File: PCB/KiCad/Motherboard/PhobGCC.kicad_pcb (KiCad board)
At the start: 2 copper layers, 125.5 x 72.9 mm, 60 parts, among them J1 Conn_01x06_Female, J2 Conn_01x04_Female, J3 Conn_01x01_Male, J5 Rumble, Q1 Q_NMOS_GSD, Q2 Q_PMOS_GDS, Q3 Q_NMOS_GSD, SW1 A, SW10 Dup, SW11 Dright, SW12 Ddown, SW2 B, SW3 X, SW4 Y, SW5 Start, SW6 L, SW7 R, SW8 Z, SW9 Dleft, U1 Teensy4.0, U2 2x DRV5053CAQLPGM Hall Effect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

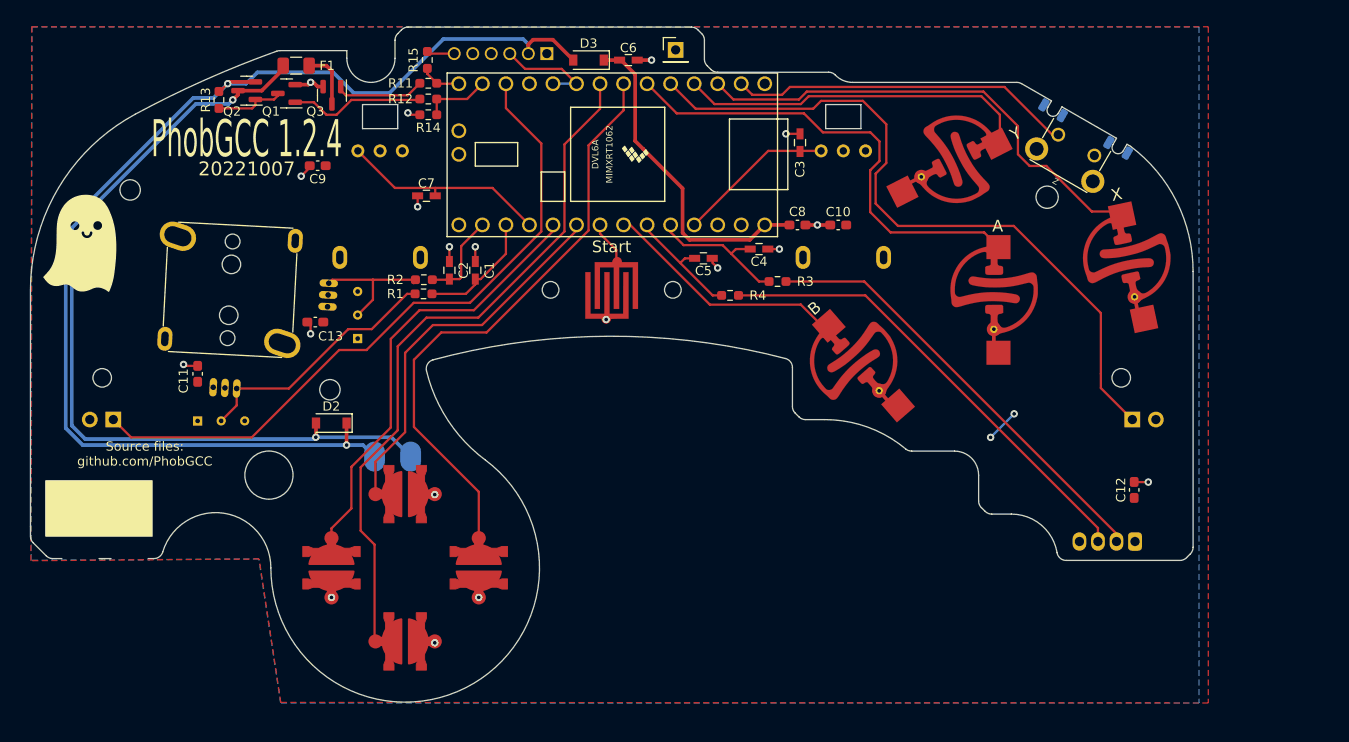
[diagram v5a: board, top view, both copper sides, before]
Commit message: elongate pads, flip wire mount cstick, z 1.1mm hole
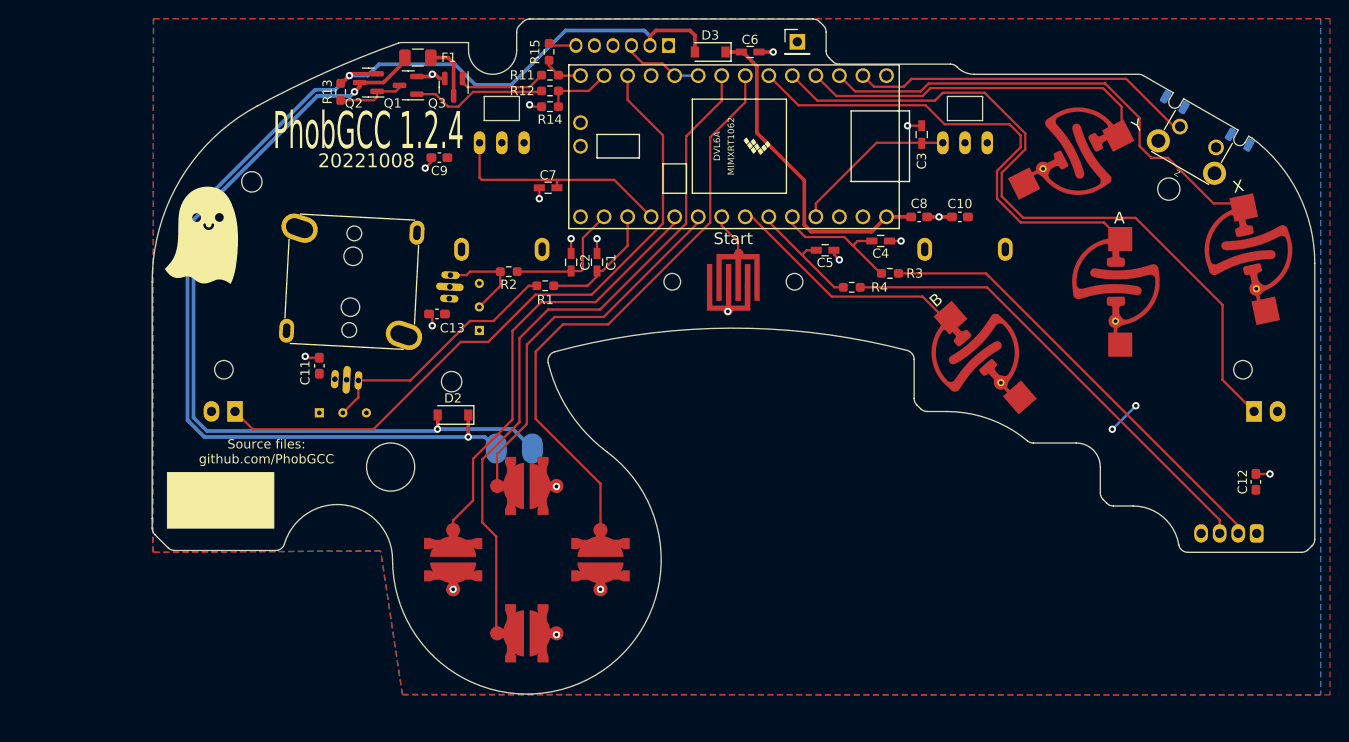
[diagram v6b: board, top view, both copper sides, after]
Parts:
- moved C1 13.2 mm to (98.4, 49.2)
- moved C10 13.2 mm to (137.6, 44.3)
- moved C12 13.2 mm to (169.5, 72.9)
- moved C6 13.2 mm to (114.9, 26.5)
- moved C8 13.2 mm to (133.2, 44.3)
- moved H2 13.2 mm to (172.9, 76.3)
- moved H9 13.2 mm to (82.7, 62.1)
- moved Q3 13.2 mm to (82.9, 30.3)
- moved SW2 13.2 mm to (139.2, 59.0)
- moved SW3 13.2 mm to (168.7, 47.9)
- moved SW7 13.2 mm to (169.3, 65.3)
- moved H3 13.2 mm to (58.1, 60.8)
- moved Q2 13.2 mm to (73.7, 29.8)
- moved R13 13.2 mm to (70.7, 30.8)
- moved TSTP1 13.2 mm to (71.0, 65.5)
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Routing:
- net /Stick_y: track 14.3 -> 10.3 mm
- net /Stick_y_filt: track 9.83 -> 13.8 mm
- net /Lanalog: track 22.7 -> 24.9 mm
- net /Data: track 11.1 -> 9.26 mm
- net /A: track 50.4 -> 52.1 mm
- net +5V: track 131.4 -> 132.6 mm
- net /C_x_filt: track 16.0 -> 14.9 mm
- net /R: track 76.9 -> 77.9 mm
- net /C_x: track 47.9 -> 48.8 mm
- net /Ranalog: track 17.0 -> 17.9 mm
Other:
- outline, holes or cut-outs redrawn
- board text added: "20221008"
- board text removed: "20221007"
